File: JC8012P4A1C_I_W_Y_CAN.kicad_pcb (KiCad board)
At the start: 6 copper layers, 66 x 54 mm, 39 parts, among them J1 610110249121, J2 68711414522, J3 653104131822, Q1 Si4948BEY, U1 TLE9250VSJ, U2 171030601

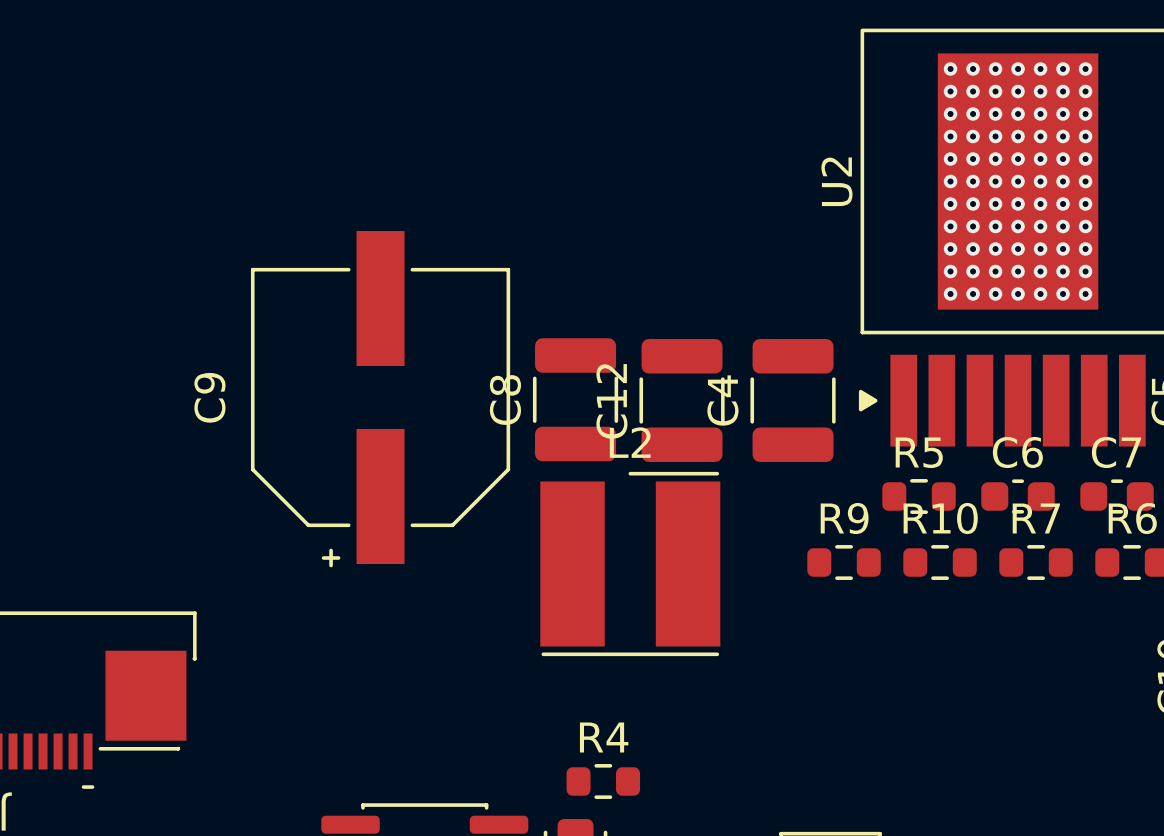
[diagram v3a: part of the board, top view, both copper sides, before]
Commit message: Separate BUCK_AGND net, no thermal reliefs for SMD pads
- New local net BUCK_AGND on the power sheet: U2 pin 4 (AGND),
  C6 (C_SS), R7 (R_FBB), R10 (R_ENB). AGND is connected to PGND inside
  the 171030601; these grounds must be routed to the AGND pin only and
  not to the GND plane (datasheet p. 41). PWR_FLAG and a note added.
- PCB pads updated accordingly (schematic parity OK)
- All zones: pad connection "thermal reliefs for PTH only", i.e. all
  SMD pads solidly connected
- Includes placement tweaks and the VIN_BUCK zone on F.Cu done in KiCad
  (C4/C12 closer to U2, L2, C8, C9 moved)

Co-Authored-By: Claude Opus 5.5 <noreply@anthropic.com>
Claude-Session: https://claude.ai/code/session_014h8cGi8SRWthYdGFH1Qgzz
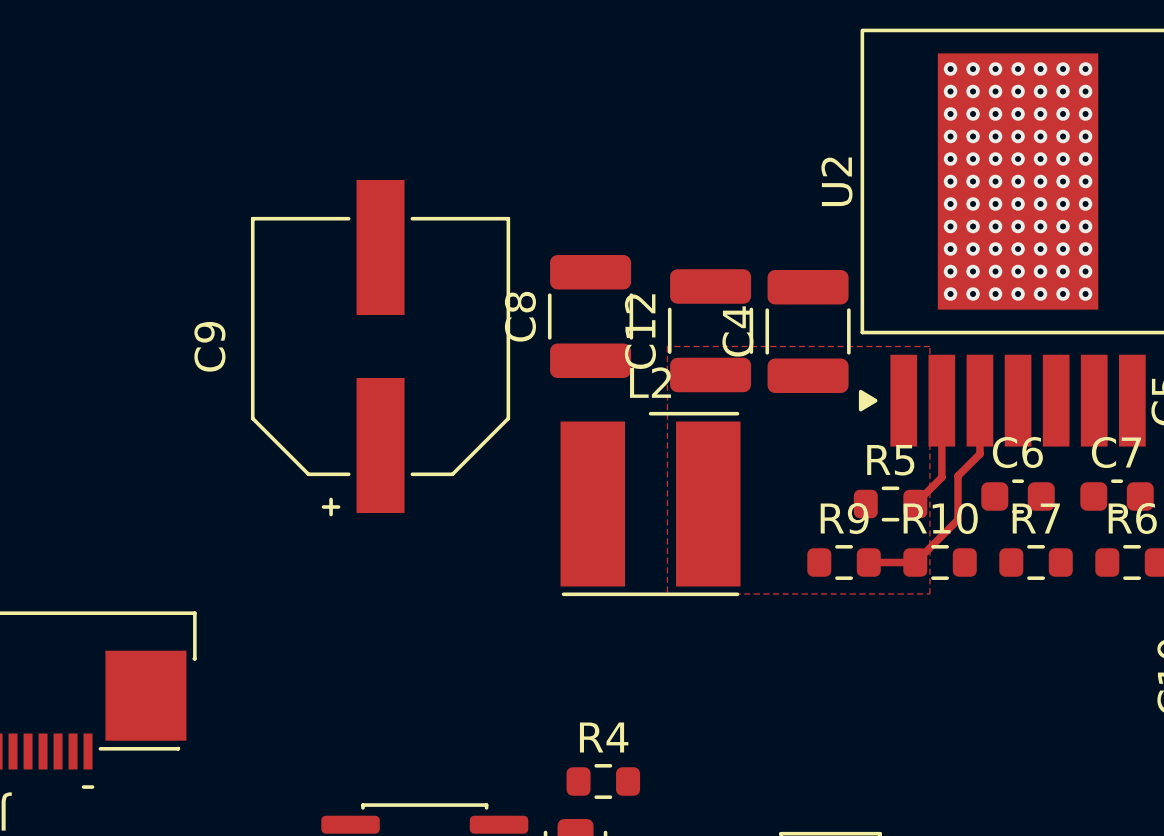
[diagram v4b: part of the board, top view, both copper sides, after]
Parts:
- moved C8 2.82 mm to (132.8, 113.0)
- moved C12 2.51 mm to (136.8, 113.5)
- moved C4 2.35 mm to (140.0, 113.5)
- moved L2 2.11 mm to (134.8, 119.2)
- moved C9 1.70 mm to (125.8, 114.0)
- moved R5 0.98 mm to (142.8, 119.2)
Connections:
- C6 pad 2: GND -> /Versorgung/BUCK_AGND
- R10 pad 2: GND -> /Versorgung/BUCK_AGND
- R7 pad 2: GND -> /Versorgung/BUCK_AGND
- U2 pad 4: GND -> /Versorgung/BUCK_AGND
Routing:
- net /Versorgung/BUCK_EN: track 0.00 -> 7.84 mm
- net /Versorgung/BUCK_RON: track 0.00 -> 3.81 mm
- added copper zone on F.Cu, net /Versorgung/VIN_BUCK
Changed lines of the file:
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@@
 	(footprint "Capacitor_SMD:C_1210_3225Metric"
 		(layer "F.Cu")
-		(at 135.8 115.8 90)
+		(at 136.75 113.475 90)
 		(descr "Capacitor SMD 1210 (3225 Metric), square (rectangular) end terminal, IPC-7351 nominal, (Body size source: IPC-SM-782 page 76, https://www.pcb-3d.com/wordpress/wp-content/uploads/ipc-sm-782a_amendment_1_and_2.pdf)")
 		(tags "capacitor")
@@
 	(footprint "JC8012P4A1C_CAN:L_Wurth_WE-PD2-5848"
 		(layer "F.Cu")
-		(at 134.075 121.25)
+		(at 134.75 119.25)
 		(descr "Unshielded Power Inductor, body 5.8x5.2x4.5mm, https://www.we-online.com/en/components/products/WE-PD2#/articles/WE-PD2-5848")
 		(tags "SMT")
@@
 			(layers "F.Cu" "F.Mask" "F.Paste")
 			(roundrect_rratio 0.25)
-			(net "GND")
+			(net "/Versorgung/BUCK_AGND")
 			(pintype "passive")
 		)
@@
 	(footprint "Capacitor_SMD:C_1210_3225Metric"
 		(layer "F.Cu")
-		(at 139.5 115.8 90)
+		(at 140 113.5 90)
 		(descr "Capacitor SMD 1210 (3225 Metric), square (rectangular) end terminal, IPC-7351 nominal, (Body size source: IPC-SM-782 page 76, https://www.pcb-3d.com/wordpress/wp-content/uploads/ipc-sm-782a_amendment_1_and_2.pdf)")
 		(tags "capacitor")
@@
 			(layers "F.Cu" "F.Mask" "F.Paste")
 			(roundrect_rratio 0.25)
-			(net "GND")
+			(net "/Versorgung/BUCK_AGND")
 			(pintype "passive")
 		)
@@
 	(footprint "JC8012P4A1C_CAN:CP_Wurth_WCAP-ASLI-D8L6.5"
 		(layer "F.Cu")
-		(at 125.75 115.7 90)
+		(at 125.75 114 90)
 		(descr "Aluminum Electrolytic Capacitors Low Impedance +105 °C, body x8x6.5mm, https://www.we-online.com/en/components/products/WCAP-ASLI#/articles/WCAP_ASLI_SIZE_8")
 		(tags "SMT")
@@
 	(footprint "Capacitor_SMD:C_1210_3225Metric"
 		(layer "F.Cu")
-		(at 132.25 115.775 90)
+		(at 132.75 113 90)
 		(descr "Capacitor SMD 1210 (3225 Metric), square (rectangular) end terminal, IPC-7351 nominal, (Body size source: IPC-SM-782 page 76, https://www.pcb-3d.com/wordpress/wp-content/uploads/ipc-sm-782a_amendment_1_and_2.pdf)")
 		(tags "capacitor")
@@
 			(size 3.06 0.89)
 			(layers "F.Cu" "F.Mask" "F.Paste")
-			(net "GND")
+			(net "/Versorgung/BUCK_AGND")
 			(pinfunction "AGND_4")
 			(pintype "power_in")
@@
 			(layers "F.Cu" "F.Mask" "F.Paste")
 			(roundrect_rratio 0.25)
-			(net "GND")
+			(net "/Versorgung/BUCK_AGND")
 			(pintype "passive")
 		)
@@
 	(footprint "Resistor_SMD:R_0603_1608Metric"
 		(layer "F.Cu")
-		(at 143.7 119)
+		(at 142.75 119.25)
 		(descr "Resistor SMD 0603 (1608 Metric), square (rectangular) end terminal, IPC-7351 nominal, (Body size source: IPC-SM-782 page 72, https://www.pcb-3d.com/wordpress/wp-content/uploads/ipc-sm-782a_amendment_1_and_2.pdf)")
 		(tags "resistor")
@@
 		(net "GND")
 	)
+	(segment
+		(start 145.73 115.805)
+		(end 145.73 117.585)
+		(width 0.25)
+		(layer "F.Cu")
+		(net "/Versorgung/BUCK_EN")
+	)
+	(segment
+		(start 145 119.775)
+		(end 143.575 121.2)
+		(width 0.25)
+		(layer "F.Cu")
+		(net "/Versorgung/BUCK_EN")
+	)
+	(segment
+		(start 145.73 117.585)
+		(end 145 118.315)
+		(width 0.25)
+		(layer "F.Cu")
+		(net "/Versorgung/BUCK_EN")
+	)
+	(segment
+		(start 145 118.315)
+		(end 145 119.775)
+		(width 0.25)
+		(layer "F.Cu")
+		(net "/Versorgung/BUCK_EN")
+	)
+	(segment
+		(start 142.025 121.2)
+		(end 143.575 121.2)
+		(width 0.25)
+		(layer "F.Cu")
+		(net "/Versorgung/BUCK_EN")
+	)
+	(segment
+		(start 144.46 115.805)
+		(end 144.46 118.365)
+		(width 0.25)
+		(layer "F.Cu")
+		(net "/Versorgung/BUCK_RON")
+	)
+	(segment
+		(start 144.46 118.365)
+		(end 143.575 119.25)
+		(width 0.25)
+		(layer "F.Cu")
+		(net "/Versorgung/BUCK_RON")
+	)
+	(zone
+		(net "/Versorgung/VIN_BUCK")
+		(layer "F.Cu")
+		(hatch edge 0.5)
+		(priority 1)
+		(connect_pads thru_hole_only
+			(clearance 0.5)
+		)
+		(min_thickness 0.25)
+		(fill yes
+			(thermal_gap 0.5)
+			(thermal_bridge_width 0.5)
+			(island_removal_mode 0)
+		)
+		(polygon
+			(pts
+				(xy 144.063286 114) (xy 135.313285 114) (xy 135.313285 122.25) (xy 144.063286 122.25)
+			)
+		)
+	)
 	(zone
 		(net "GND")
 		(layer "F.Cu")
 		(hatch edge 0.5)
-		(connect_pads
+		(connect_pads thru_hole_only
 			(clearance 0.3)
 		)
@@
 		(layer "B.Cu")
 		(hatch edge 0.5)
-		(connect_pads
+		(connect_pads thru_hole_only
 			(clearance 0.3)
 		)
@@
 		(layer "In1.Cu")
 		(hatch edge 0.5)
-		(connect_pads
+		(connect_pads thru_hole_only
 			(clearance 0.3)
 		)
@@
 		(layer "In2.Cu")
 		(hatch edge 0.5)
-		(connect_pads
+		(connect_pads thru_hole_only
 			(clearance 0.3)
 		)
@@
 		(layer "In4.Cu")
 		(hatch edge 0.5)
-		(connect_pads
+		(connect_pads thru_hole_only
 			(clearance 0.3)
 		)

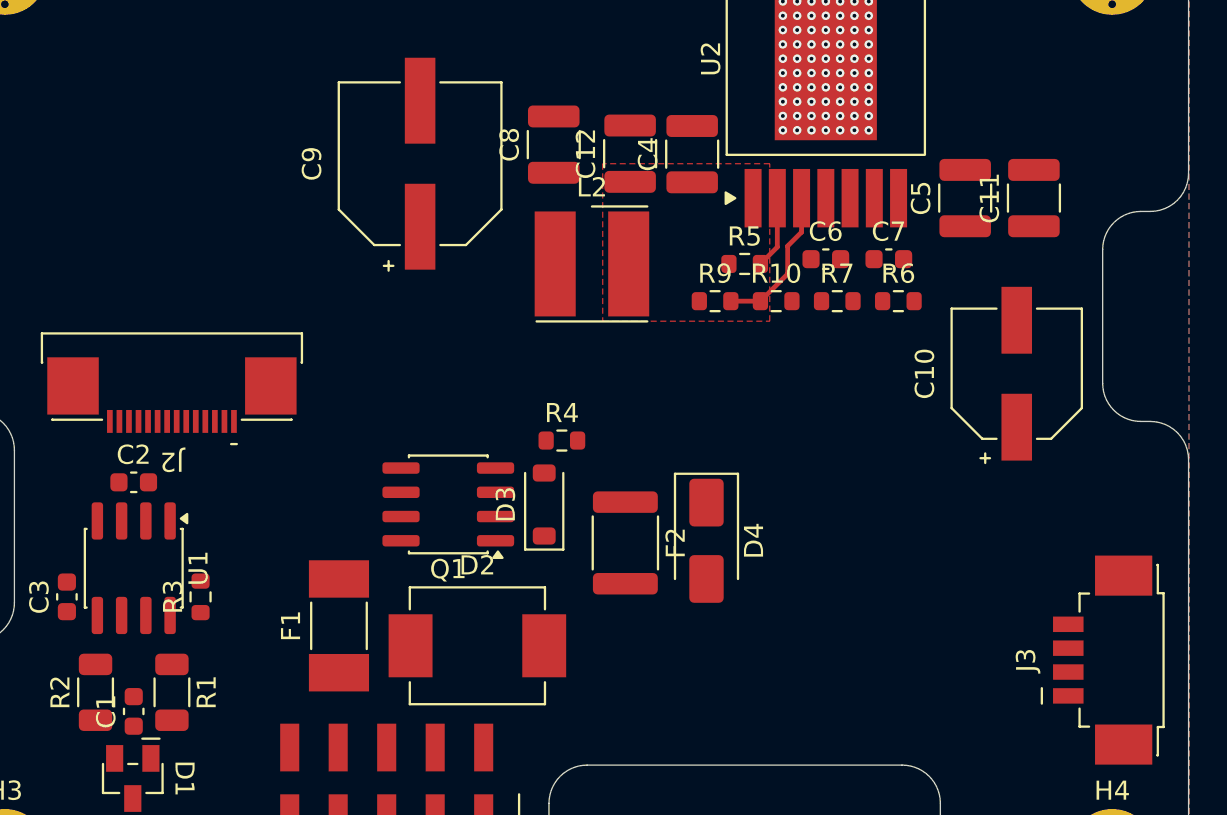
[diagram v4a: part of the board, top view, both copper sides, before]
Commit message: Buck converter routing done in KiCad, +5V vias, C10 on the +5V zone
- Converter routing (KiCad): RON, EN, SS, FB, AGND star to pin 4,
  VIN_BUCK zone and +5V zone on F.Cu, C10 rotated (+ towards VOUT)
- 6 vias from the +5V zone to the In2 +5V plane, vias in C10+, J3 pin 1,
  C2 pin 1 and U1 pin 3 (+5V plane now connected)
- 2 GND vias each in the GND pads of C4, C12, C5, C11
- FB sense line C11+ -> R6/C7 reduced to 0.3 mm
- +5V zone on F.Cu extended so that C10 (polymer) sits on the same
  copper as C5/C11 and U2 pin 7 (as on the evaluation board)
- New +5V zone also "thermal reliefs for PTH only"
- All vias 0.45/0.2 mm (epoxy filled & capped at JLCPCB)

Co-Authored-By: Claude Opus 5.5 <noreply@anthropic.com>
Claude-Session: https://claude.ai/code/session_014h8cGi8SRWthYdGFH1Qgzz
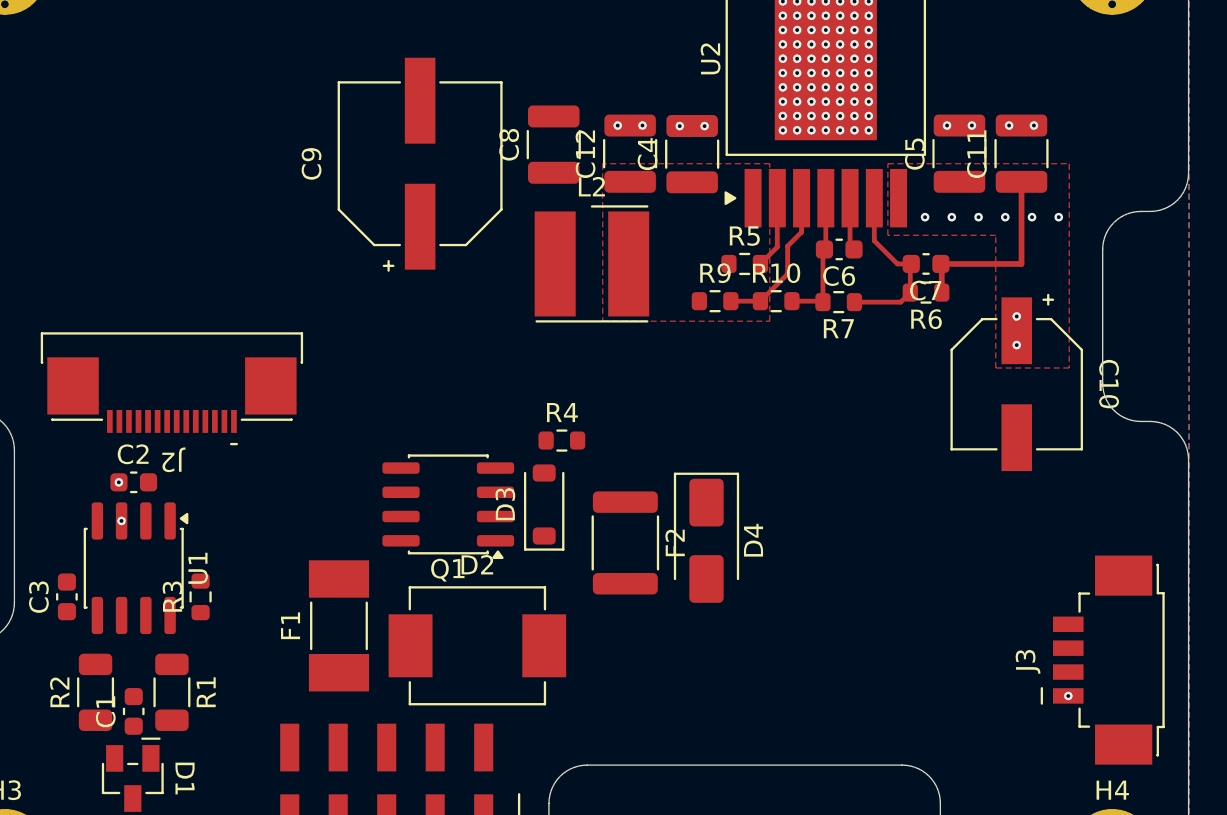
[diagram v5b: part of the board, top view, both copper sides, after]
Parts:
- moved C11 2.41 mm to (157.2, 113.5)
- moved C5 2.34 mm to (154.0, 113.5)
- moved C7 1.97 mm to (152.2, 119.2), turned to 180 degrees
- moved R6 1.52 mm to (152.2, 120.8), turned to 180 degrees
- moved C6 0.87 mm to (147.7, 118.5), turned to 180 degrees
- moved C10 0.55 mm to (157.0, 125.5), turned to -90 degrees
- moved R7 0.09 mm to (147.7, 121.2), turned to 180 degrees
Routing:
- net +5V: track 0.00 -> 10.0 mm, vias 0 -> 11
- net /Versorgung/BUCK_FB: track 0.00 -> 9.32 mm
- net /Versorgung/BUCK_AGND: track 0.00 -> 7.15 mm
- net /Versorgung/BUCK_SS: track 0.00 -> 2.77 mm
- net GND: vias 77 -> 85
- added copper zone on F.Cu, net +5V

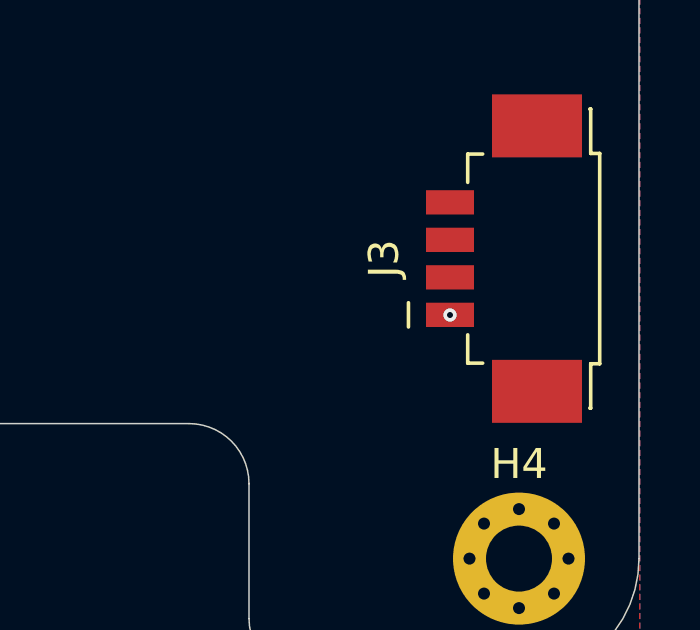
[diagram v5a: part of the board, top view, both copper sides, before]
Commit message: J3 +5V pad: two vias instead of one
Pin 1 of J3 carries the whole display current from the In2 +5V plane.
Replace the single 0.45/0.2 via by two vias inside the pad.

Co-Authored-By: Claude Opus 5.5 <noreply@anthropic.com>
Claude-Session: https://claude.ai/code/session_014h8cGi8SRWthYdGFH1Qgzz
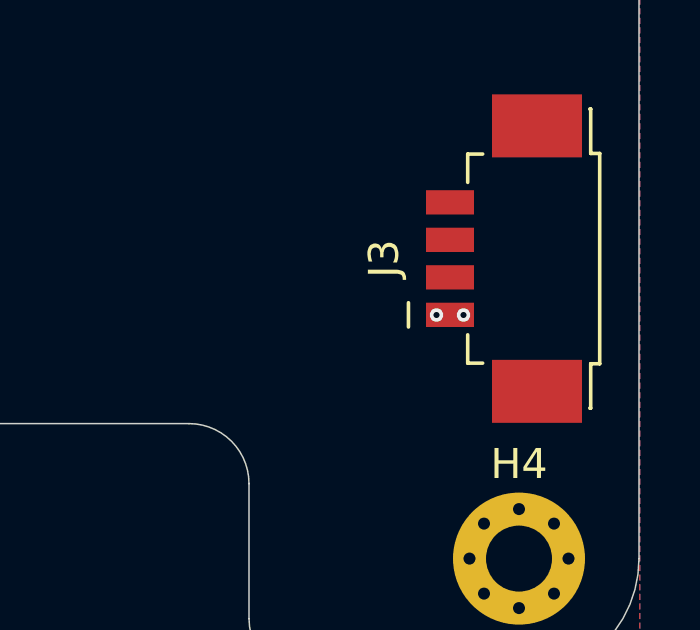
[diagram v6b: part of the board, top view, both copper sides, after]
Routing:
- net +5V: vias 11 -> 12
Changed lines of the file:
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@@
 	)
 	(via
-		(at 159.7 141.88)
+		(at 155 116.8)
 		(size 0.45)
 		(drill 0.2)
@@
 	)
 	(via
-		(at 155 116.8)
+		(at 160.15 141.88)
 		(size 0.45)
 		(drill 0.2)
+		(layers "F.Cu" "B.Cu")
+		(net "+5V")
+	)
+	(via
+		(at 159.25 141.88)
+		(size 0.45)
+		(drill 0.2)
